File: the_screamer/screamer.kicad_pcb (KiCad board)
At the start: 4 copper layers, 18 x 10 mm, 14 parts, among them U1 TC2185-3.3VxCTTR, U2 MAX2606

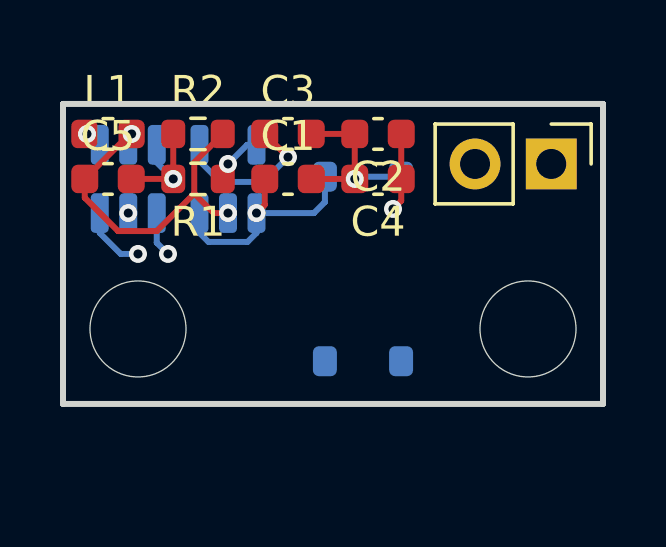
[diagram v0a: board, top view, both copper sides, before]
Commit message: Added connector to Screamer
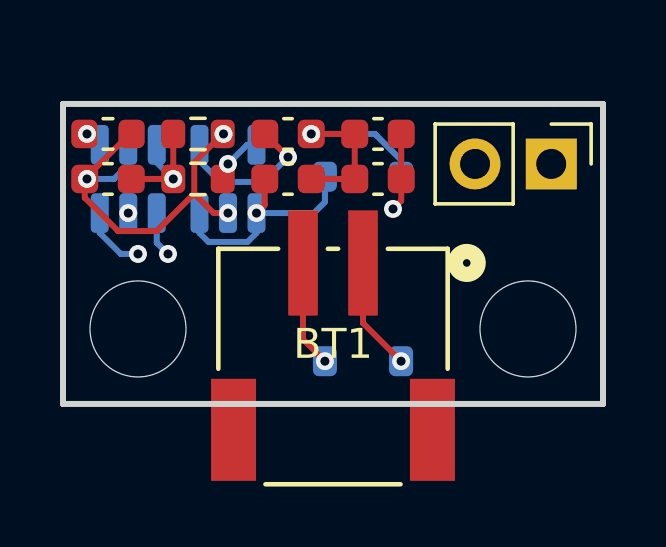
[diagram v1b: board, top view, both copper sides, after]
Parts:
- added BT1: Battery_Cell, locals but working PLEASE:JST_CONN2_1775469-2_TEC, F.Cu at (159.0, 95.3)
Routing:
- net GND: track 17.6 -> 24.8 mm, vias 3 -> 4
- net Net-(BT1-+): track 0.00 -> 3.80 mm, vias 0 -> 1
- net Net-(BT1--): track 0.00 -> 3.58 mm, vias 0 -> 1
